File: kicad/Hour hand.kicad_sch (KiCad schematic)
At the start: 66 parts, among them U001 74HC595, U002 74HC595

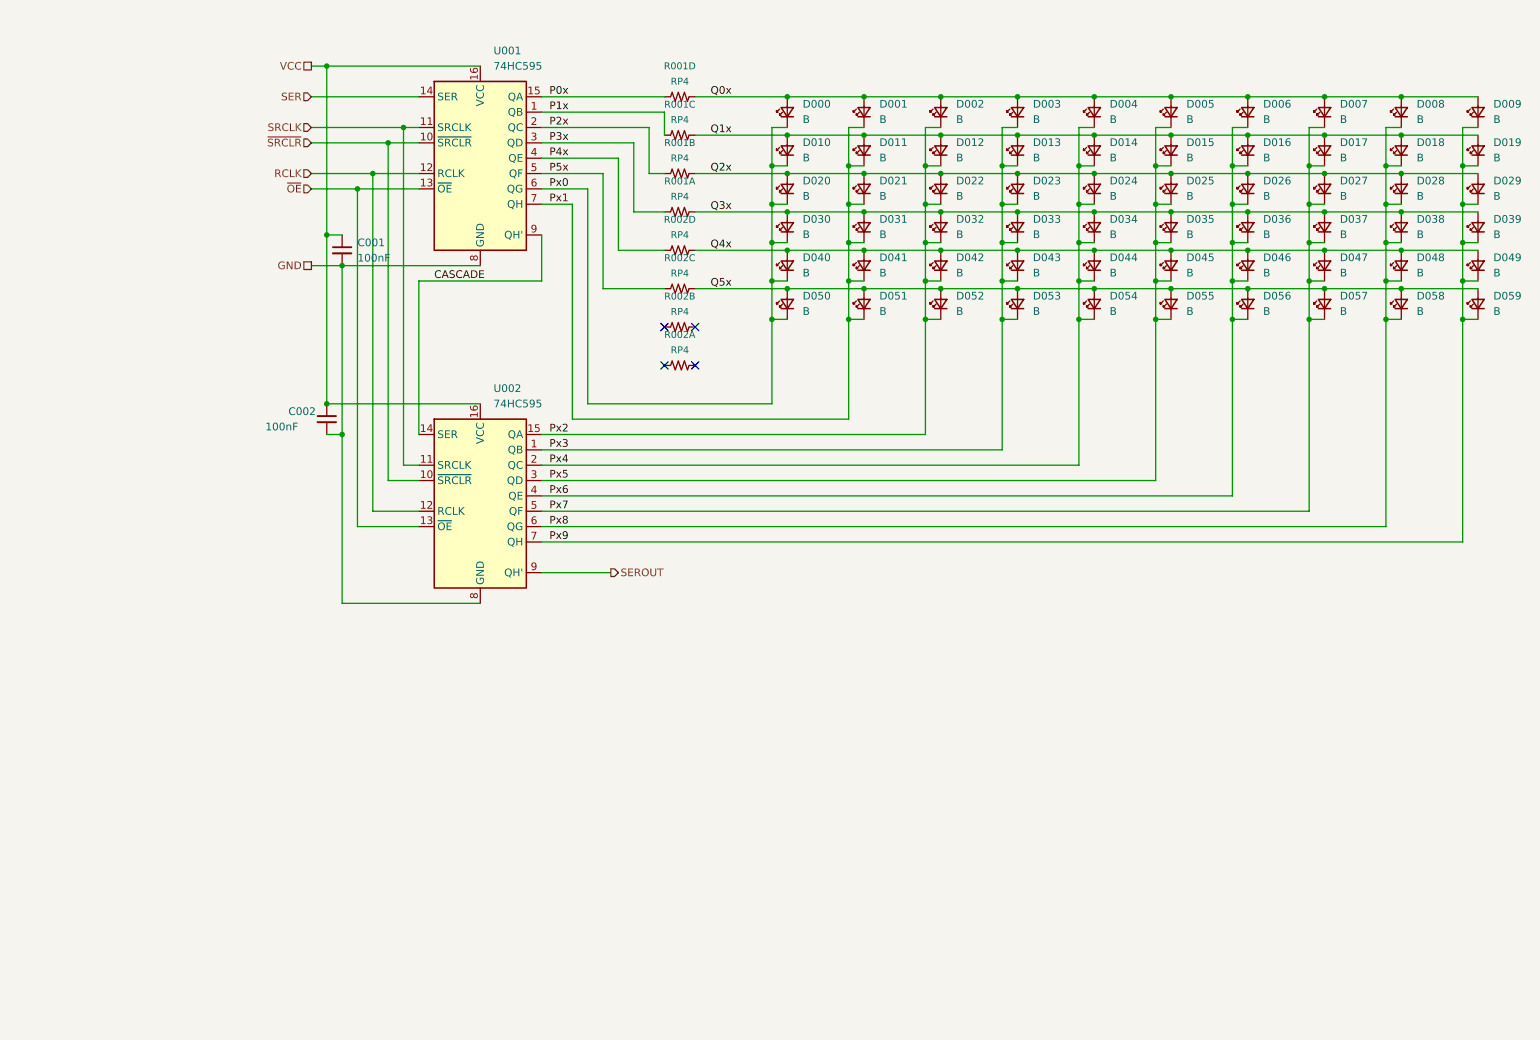
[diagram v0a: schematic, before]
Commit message: Updated to 3 multiplexers
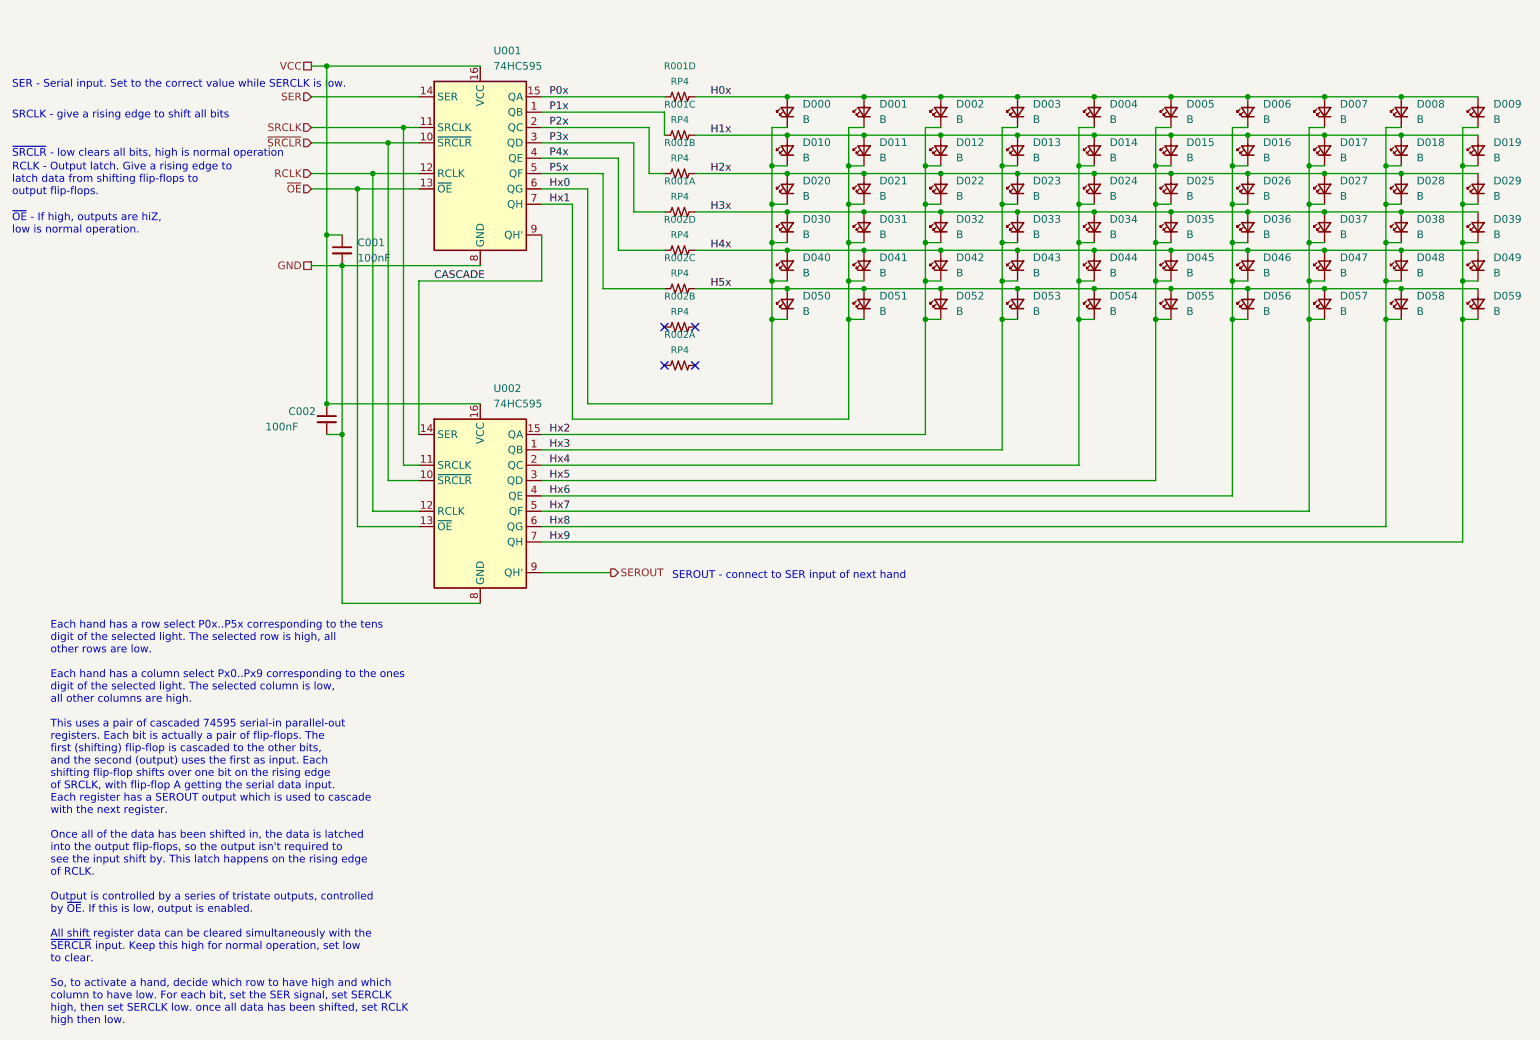
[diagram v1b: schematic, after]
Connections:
- net Px0 renamed Hx0
- net Px1 renamed Hx1
- net Px2 renamed Hx2
- net Px3 renamed Hx3
- net Px4 renamed Hx4
- net Px5 renamed Hx5
- net Px6 renamed Hx6
- net Px7 renamed Hx7
- net Px8 renamed Hx8
- net Px9 renamed Hx9
- net Q0x renamed H0x
- net Q1x renamed H1x
- net Q2x renamed H2x
- net Q3x renamed H3x
- net Q4x renamed H4x
- net Q5x renamed H5x
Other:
- note added: "Each hand has a row select P0x..P5x corresponding to the tens digit of the selected light. The selected row is high, all other rows are low. Each hand has a column select Px0..Px9 corresponding to the ones digit of the selected light. The selected column is low, all other columns are high. This uses a pair of cascaded 74595 serial-in parallel-out registers. Each bit is actually a pair of flip-flo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"
- note added: "RCLK - Output latch. Give a rising edge to latch data from shifting flip-flops to output flip-flops."
- note added: "SER - Serial input. Set to the correct value while SERCLK is low."
- note added: "SEROUT - connect to SER input of next hand"
- note added: "SRCLK - give a rising edge to shift all bits"
- note added: "~{OE} - If high, outputs are hiZ, low is normal operation."
- note added: "~{SRCLR} - low clears all bits, high is normal operation"
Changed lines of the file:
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@@
     (stroke (width 0) (type default))
+  )
+  (text "Each hand has a row select P0x..P5x corresponding to the tens\ndigit of the selected light. The selected row is high, all \nother rows are low.\n\nEach hand has a column select Px0..Px9 corresponding to the ones\ndigit of the selected light. The selected column is low, \nall other columns are high.\n\nThis uses a pair of cascaded 74595 serial-in parallel-out \nregisters. Each bit is actually a pair of flip-flops. The\nfirst (shifting) flip-flop is cascaded to the other bits,\nand the second (output) uses the first as input. Each \nshifting flip-flop shifts over one bit on the rising edge\nof SRCLK, with flip-flop A getting the serial data input.\nEach register has a SEROUT output which is used to cascade\nwith the next register.\n\nOnce all of the data has been shifted in, the data is latched\ninto the output flip-flops, so the output isn't required to\nsee the input shift by. This latch happens on the rising edge\nof RCLK.\n\nOutput is controlled by a series of tristate outputs, controlled\nby ~{OE}. If this is low, output is enabled.\n\nAll shift register data can be cleared simultaneously with the\n~{SERCLR} input. Keep this high for normal operation, set low\nto clear.\n\nSo, to activate a hand, decide which row to have high and which\ncolumn to have low. For each bit, set the SER signal, set SERCLK\nhigh, then set SERCLK low. once all data has been shifted, set RCLK\nhigh then low."
+    (at 20.32 191.77 0)
+    (effects (font (size 1.27 1.27)) (justify left bottom))
+  )
+  (text "RCLK - Output latch. Give a rising edge to\nlatch data from shifting flip-flops to \noutput flip-flops."
+    (at 13.97 54.61 0)
+    (effects (font (size 1.27 1.27)) (justify left bottom))
+  )
+  (text "SEROUT - connect to SER input of next hand" (at 123.19 118.11 0)
+    (effects (font (size 1.27 1.27)) (justify left bottom))
+  )
+  (text "SER - Serial input. Set to the correct value while SERCLK is low."
+    (at 13.97 36.83 0)
+    (effects (font (size 1.27 1.27)) (justify left bottom))
+  )
+  (text "~{OE} - If high, outputs are hiZ, \nlow is normal operation."
+    (at 13.97 60.96 0)
+    (effects (font (size 1.27 1.27)) (justify left bottom))
+  )
+  (text "SRCLK - give a rising edge to shift all bits" (at 13.97 41.91 0)
+    (effects (font (size 1.27 1.27)) (justify left bottom))
+  )
+  (text "~{SRCLR} - low clears all bits, high is normal operation"
+    (at 13.97 48.26 0)
+    (effects (font (size 1.27 1.27)) (justify left bottom))
   )
   (label "P2x" (at 102.87 43.18 0) (fields_autoplaced)
     (effects (font (size 1.27 1.27)) (justify left bottom))
   )
-  (label "Px6" (at 102.87 104.14 0) (fields_autoplaced)
+  (label "Hx6" (at 102.87 104.14 0) (fields_autoplaced)
     (effects (font (size 1.27 1.27)) (justify left bottom))
   )
-  (label "Q1x" (at 129.54 44.45 0) (fields_autoplaced)
+  (label "H1x" (at 129.54 44.45 0) (fields_autoplaced)
     (effects (font (size 1.27 1.27)) (justify left bottom))
   )
@@
     (effects (font (size 1.27 1.27)) (justify left bottom))
   )
-  (label "Px2" (at 102.87 93.98 0) (fields_autoplaced)
+  (label "Hx2" (at 102.87 93.98 0) (fields_autoplaced)
     (effects (font (size 1.27 1.27)) (justify left bottom))
   )
@@
     (effects (font (size 1.27 1.27)) (justify left bottom))
   )
-  (label "Px1" (at 102.87 55.88 0) (fields_autoplaced)
+  (label "Hx1" (at 102.87 55.88 0) (fields_autoplaced)
     (effects (font (size 1.27 1.27)) (justify left bottom))
   )
-  (label "Q2x" (at 129.54 50.8 0) (fields_autoplaced)
+  (label "H2x" (at 129.54 50.8 0) (fields_autoplaced)
     (effects (font (size 1.27 1.27)) (justify left bottom))
   )
-  (label "Q3x" (at 129.54 57.15 0) (fields_autoplaced)
+  (label "H3x" (at 129.54 57.15 0) (fields_autoplaced)
     (effects (font (size 1.27 1.27)) (justify left bottom))
   )
-  (label "Px7" (at 102.87 106.68 0) (fields_autoplaced)
+  (label "Hx7" (at 102.87 106.68 0) (fields_autoplaced)
     (effects (font (size 1.27 1.27)) (justify left bottom))
   )
@@
     (effects (font (size 1.27 1.27)) (justify left bottom))
   )
-  (label "Px0" (at 102.87 53.34 0) (fields_autoplaced)
+  (label "Hx0" (at 102.87 53.34 0) (fields_autoplaced)
     (effects (font (size 1.27 1.27)) (justify left bottom))
   )
-  (label "Px3" (at 102.87 96.52 0) (fields_autoplaced)
+  (label "Hx3" (at 102.87 96.52 0) (fields_autoplaced)
     (effects (font (size 1.27 1.27)) (justify left bottom))
   )
-  (label "Q0x" (at 129.54 38.1 0) (fields_autoplaced)
+  (label "H0x" (at 129.54 38.1 0) (fields_autoplaced)
     (effects (font (size 1.27 1.27)) (justify left bottom))
   )
-  (label "Px8" (at 102.87 109.22 0) (fields_autoplaced)
+  (label "Hx8" (at 102.87 109.22 0) (fields_autoplaced)
     (effects (font (size 1.27 1.27)) (justify left bottom))
   )
-  (label "Q4x" (at 129.54 63.5 0) (fields_autoplaced)
+  (label "H4x" (at 129.54 63.5 0) (fields_autoplaced)
     (effects (font (size 1.27 1.27)) (justify left bottom))
   )
-  (label "Px4" (at 102.87 99.06 0) (fields_autoplaced)
+  (label "Hx4" (at 102.87 99.06 0) (fields_autoplaced)
     (effects (font (size 1.27 1.27)) (justify left bottom))
   )
-  (label "Q5x" (at 129.54 69.85 0) (fields_autoplaced)
+  (label "H5x" (at 129.54 69.85 0) (fields_autoplaced)
     (effects (font (size 1.27 1.27)) (justify left bottom))
   )
-  (label "Px5" (at 102.87 101.6 0) (fields_autoplaced)
+  (label "Hx5" (at 102.87 101.6 0) (fields_autoplaced)
     (effects (font (size 1.27 1.27)) (justify left bottom))
   )
-  (label "Px9" (at 102.87 111.76 0) (fields_autoplaced)
+  (label "Hx9" (at 102.87 111.76 0) (fields_autoplaced)
     (effects (font (size 1.27 1.27)) (justify left bottom))
   )

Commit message: First completely routed version
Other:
- note added: "D2"
- note added: "D3"
- note added: "D4"
- note added: "D5"
- note added: "D6"
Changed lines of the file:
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@@
     (stroke (width 0) (type default))
+  )
+  (text "D6" (at 53.34 54.61 0)
+    (effects (font (size 1.27 1.27)) (justify left bottom))
   )
   (text "Each hand has a row select P0x..P5x corresponding to the tens\ndigit of the selected light. The selected row is high, all \nother rows are low.\n\nEach hand has a column select Px0..Px9 corresponding to the ones\ndigit of the selected light. The selected column is low, \nall other columns are high.\n\nThis uses a pair of cascaded 74595 serial-in parallel-out \nregisters. Each bit is actually a pair of flip-flops. The\nfirst (shifting) flip-flop is cascaded to the other bits,\nand the second (output) uses the first as input. Each \nshifting flip-flop shifts over one bit on the rising edge\nof SRCLK, with flip-flop A getting the serial data input.\nEach register has a SEROUT output which is used to cascade\nwith the next register.\n\nOnce all of the data has been shifted in, the data is latched\ninto the output flip-flops, so the output isn't required to\nsee the input shift by. This latch happens on the rising edge\nof RCLK.\n\nOutput is controlled by a series of tristate outputs, controlled\nby ~{OE}. If this is low, output is enabled.\n\nAll shift register data can be cleared simultaneously with the\n~{SERCLR} input. Keep this high for normal operation, set low\nto clear.\n\nSo, to activate a hand, decide which row to have high and which\ncolumn to have low. For each bit, set the SER signal, set SERCLK\nhigh, then set SERCLK low. once all data has been shifted, set RCLK\nhigh then low."
@@
     (effects (font (size 1.27 1.27)) (justify left bottom))
   )
+  (text "D3" (at 53.34 44.45 0)
+    (effects (font (size 1.27 1.27)) (justify left bottom))
+  )
   (text "SEROUT - connect to SER input of next hand" (at 123.19 118.11 0)
+    (effects (font (size 1.27 1.27)) (justify left bottom))
+  )
+  (text "D5" (at 53.34 52.07 0)
     (effects (font (size 1.27 1.27)) (justify left bottom))
   )
@@
     (effects (font (size 1.27 1.27)) (justify left bottom))
   )
+  (text "D2" (at 53.34 39.37 0)
+    (effects (font (size 1.27 1.27)) (justify left bottom))
+  )
+  (text "D4" (at 53.34 46.99 0)
+    (effects (font (size 1.27 1.27)) (justify left bottom))
+  )

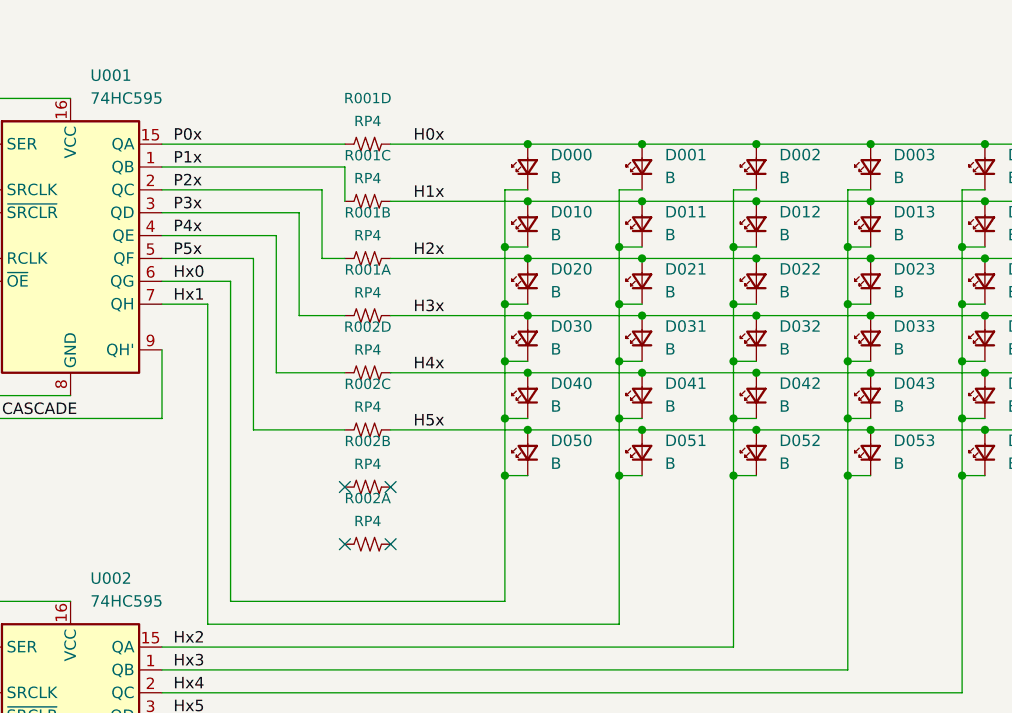
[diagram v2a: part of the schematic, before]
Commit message: Add notes for diode voltages
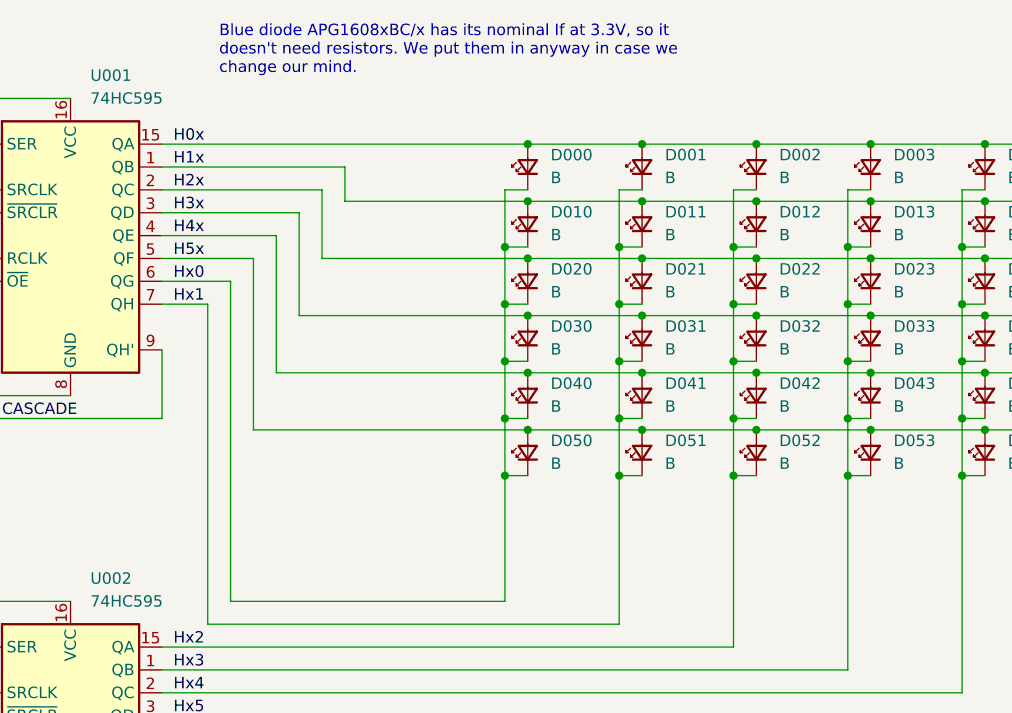
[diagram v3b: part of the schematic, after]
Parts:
- removed R001, R002: RP4, KwanSystems:R_Array_Convex_4x0402, symbol KwanSystems:RP4
- C001, C002: Digikey (none) -> 445-5613-1-ND; Part Number (none) -> CGA2B1X7R1C104K050BC; Purpose (none) -> Hour hand decoder bypass
- D000, D001, D002, D003, D004, D005, D006, D007, D008, D009, D010, D011, D012, D013, D014, D015, D016, D017, D018, D019, D020, D021, D022, D023, D024, D025, D026, D027, D028, D029, D030, D031, D032, D033, D034, D035, D036, D037, D038, D039, D040, D041, D042, D043, D044, D045, D046, D047, D048, D049, D050, D051, D052, D053, D054, D055, D056, D057, D058, D059: Digikey 754-1434-1-ND -> 754-1351-1-ND; Part Number APT1608QBC/D -> APG1608QBC/D; Purpose (none) -> Blue hour hand
- U001, U002: Part Number (none) -> 74HC595PW,118; Purpose (none) -> Hand Decoder
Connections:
- net P0x is gone; now on net H0x: U001.15 (QA)
- net P1x is gone; now on net H1x: U001.1 (QB)
- net P2x is gone; now on net H2x: U001.2 (QC)
- net P3x is gone; now on net H3x: U001.3 (QD)
- net P4x is gone; now on net H4x: U001.4 (QE)
- net P5x is gone; now on net H5x: U001.5 (QF)
- no-connect marks 4 -> 0
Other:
- note added: "Blue diode APG1608xBC/x has its nominal If at 3.3V, so it doesn't need resistors. We put them in anyway in case we change our mind."
